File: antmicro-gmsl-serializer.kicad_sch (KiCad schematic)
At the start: 0 parts

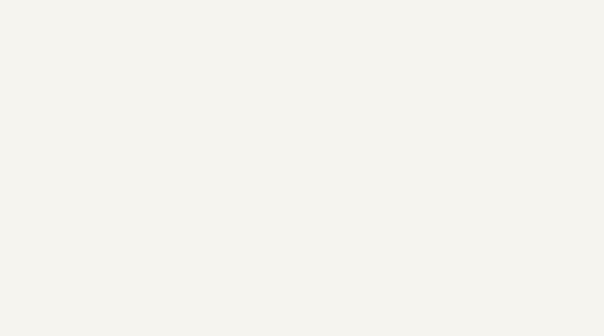
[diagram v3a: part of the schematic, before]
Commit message: Import layer stack, add mounting points
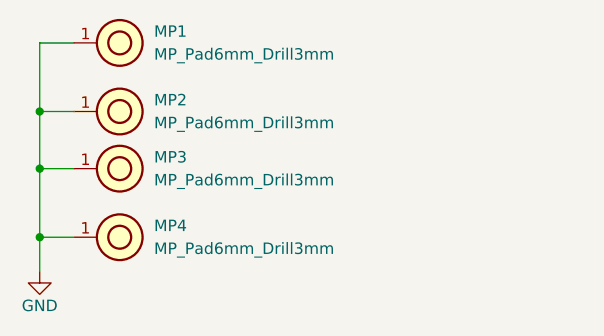
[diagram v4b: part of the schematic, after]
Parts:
- added MP1, MP2, MP3, MP4: MP_Pad6mm_Drill3mm, antmicro-footprints:MP_Pad6mm_Drill3mm, symbol antmicroMechanicalParts:MP_Pad6mm_Drill3mm
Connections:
- new net GND: MP1.1, MP2.1, MP3.1, MP4.1
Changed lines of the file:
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@@
     (comment 1 "www.antmicro.com")
+  )
+  (junction (at 24.13 157.48) (diameter 0) (color 0 0 0 0)
+  )
+  (junction (at 24.13 143.51) (diameter 0) (color 0 0 0 0)
+  )
+  (junction (at 24.13 149.86) (diameter 0) (color 0 0 0 0)
+  )
+  (wire (pts (xy 27.94 135.89) (xy 24.13 135.89))
+    (stroke (width 0) (type default) (color 0 0 0 0))
+  )
+  (wire (pts (xy 24.13 157.48) (xy 24.13 161.29))
+    (stroke (width 0) (type default) (color 0 0 0 0))
+  )
+  (wire (pts (xy 27.94 143.51) (xy 24.13 143.51))
+    (stroke (width 0) (type default) (color 0 0 0 0))
+  )
+  (wire (pts (xy 24.13 135.89) (xy 24.13 143.51))
+    (stroke (width 0) (type default) (color 0 0 0 0))
+  )
+  (wire (pts (xy 24.13 143.51) (xy 24.13 149.86))
+    (stroke (width 0) (type default) (color 0 0 0 0))
+  )
+  (wire (pts (xy 27.94 157.48) (xy 24.13 157.48))
+    (stroke (width 0) (type default) (color 0 0 0 0))
+  )
+  (wire (pts (xy 27.94 149.86) (xy 24.13 149.86))
+    (stroke (width 0) (type default) (color 0 0 0 0))
+  )
+  (wire (pts (xy 24.13 149.86) (xy 24.13 157.48))
+    (stroke (width 0) (type default) (color 0 0 0 0))
   )
   (image (at 71.12 185.674) (scale 0.15)
@@
     )
   )
+  (symbol (lib_id "antmicroMechanicalParts:MP_Pad6mm_Drill3mm") (at 27.94 157.48 0) (unit 1)
+    (in_bom yes) (on_board yes) (fields_autoplaced)
+    (property "Reference" "MP4" (id 0) (at 36.83 156.2099 0)
+      (effects (font (size 1.27 1.27) (thickness 0.15)) (justify left))
+    )
+    (property "Value" "MP_Pad6mm_Drill3mm" (id 1) (at 36.83 158.7499 0)
+      (effects (font (size 1.27 1.27) (thickness 0.15)) (justify left))
+    )
+    (property "Footprint" "antmicro-footprints:MP_Pad6mm_Drill3mm" (id 2) (at 48.26 165.1 0)
+      (effects (font (size 1.27 1.27) (thickness 0.15)) (justify left bottom) hide)
+    )
+    (property "Datasheet" "" (id 3) (at 44.78 173.05 0)
+      (effects (font (size 1.27 1.27) (thickness 0.15)) (justify left bottom) hide)
+    )
+    (property "Author" "Antmicro" (id 4) (at 48.26 167.64 0)
+      (effects (font (size 1.27 1.27) (thickness 0.15)) (justify left bottom) hide)
+    )
+    (property "License" "Apache-2.0" (id 5) (at 48.26 170.18 0)
+      (effects (font (size 1.27 1.27) (thickness 0.15)) (justify left bottom) hide)
+    )
+    (pin "1")
+  )
+  (symbol (lib_id "antmicroMechanicalParts:MP_Pad6mm_Drill3mm") (at 27.94 135.89 0) (unit 1)
+    (in_bom yes) (on_board yes) (fields_autoplaced)
+    (property "Reference" "MP1" (id 0) (at 36.83 134.6199 0)
+      (effects (font (size 1.27 1.27) (thickness 0.15)) (justify left))
+    )
+    (property "Value" "MP_Pad6mm_Drill3mm" (id 1) (at 36.83 137.1599 0)
+      (effects (font (size 1.27 1.27) (thickness 0.15)) (justify left))
+    )
+    (property "Footprint" "antmicro-footprints:MP_Pad6mm_Drill3mm" (id 2) (at 48.26 143.51 0)
+      (effects (font (size 1.27 1.27) (thickness 0.15)) (justify left bottom) hide)
+    )
+    (property "Datasheet" "" (id 3) (at 44.78 151.46 0)
+      (effects (font (size 1.27 1.27) (thickness 0.15)) (justify left bottom) hide)
+    )
+    (property "Author" "Antmicro" (id 4) (at 48.26 146.05 0)
+      (effects (font (size 1.27 1.27) (thickness 0.15)) (justify left bottom) hide)
+    )
+    (property "License" "Apache-2.0" (id 5) (at 48.26 148.59 0)
+      (effects (font (size 1.27 1.27) (thickness 0.15)) (justify left bottom) hide)
+    )
+    (pin "1")
+  )
+  (symbol (lib_id "antmicroMechanicalParts:MP_Pad6mm_Drill3mm") (at 27.94 143.51 0) (unit 1)
+    (in_bom yes) (on_board yes) (fields_autoplaced)
+    (property "Reference" "MP2" (id 0) (at 36.83 142.2399 0)
+      (effects (font (size 1.27 1.27) (thickness 0.15)) (justify left))
+    )
+    (property "Value" "MP_Pad6mm_Drill3mm" (id 1) (at 36.83 144.7799 0)
+      (effects (font (size 1.27 1.27) (thickness 0.15)) (justify left))
+    )
+    (property "Footprint" "antmicro-footprints:MP_Pad6mm_Drill3mm" (id 2) (at 48.26 151.13 0)
+      (effects (font (size 1.27 1.27) (thickness 0.15)) (justify left bottom) hide)
+    )
+    (property "Datasheet" "" (id 3) (at 44.78 159.08 0)
+      (effects (font (size 1.27 1.27) (thickness 0.15)) (justify left bottom) hide)
+    )
+    (property "Author" "Antmicro" (id 4) (at 48.26 153.67 0)
+      (effects (font (size 1.27 1.27) (thickness 0.15)) (justify left bottom) hide)
+    )
+    (property "License" "Apache-2.0" (id 5) (at 48.26 156.21 0)
+      (effects (font (size 1.27 1.27) (thickness 0.15)) (justify left bottom) hide)
+    )
+    (pin "1")
+  )
+  (symbol (lib_id "antmicropower:GND") (at 24.13 161.29 0) (unit 1)
+    (in_bom yes) (on_board yes)
+    (property "Reference" "#PWR0157" (id 0) (at 33.02 163.83 0)
+      (effects (font (size 1.27 1.27) (thickness 0.15)) (justify left bottom) hide)
+    )
+    (property "Value" "GND" (id 1) (at 24.13 165.1 0)
+      (effects (font (size 1.27 1.27) (thickness 0.15)))
+    )
+    (property "Footprint" "" (id 2) (at 33.02 168.91 0)
+      (effects (font (size 1.27 1.27) (thickness 0.15)) (justify left bottom) hide)
+    )
+    (property "Datasheet" "" (id 3) (at 33.02 173.99 0)
+      (effects (font (size 1.27 1.27) (thickness 0.15)) (justify left bottom) hide)
+    )
+    (property "Author" "Antmicro" (id 4) (at 33.02 168.91 0)
+      (effects (font (size 1.27 1.27) (thickness 0.15)) (justify left bottom) hide)
+    )
+    (property "License" "Apache-2.0" (id 5) (at 33.02 171.45 0)
+      (effects (font (size 1.27 1.27) (thickness 0.15)) (justify left bottom) hide)
+    )
+    (pin "1")
+  )
+  (symbol (lib_id "antmicroMechanicalParts:MP_Pad6mm_Drill3mm") (at 27.94 149.86 0) (unit 1)
+    (in_bom yes) (on_board yes) (fields_autoplaced)
+    (property "Reference" "MP3" (id 0) (at 36.83 148.5899 0)
+      (effects (font (size 1.27 1.27) (thickness 0.15)) (justify left))
+    )
+    (property "Value" "MP_Pad6mm_Drill3mm" (id 1) (at 36.83 151.1299 0)
+      (effects (font (size 1.27 1.27) (thickness 0.15)) (justify left))
+    )
+    (property "Footprint" "antmicro-footprints:MP_Pad6mm_Drill3mm" (id 2) (at 48.26 157.48 0)
+      (effects (font (size 1.27 1.27) (thickness 0.15)) (justify left bottom) hide)
+    )
+    (property "Datasheet" "" (id 3) (at 44.78 165.43 0)
+      (effects (font (size 1.27 1.27) (thickness 0.15)) (justify left bottom) hide)
+    )
+    (property "Author" "Antmicro" (id 4) (at 48.26 160.02 0)
+      (effects (font (size 1.27 1.27) (thickness 0.15)) (justify left bottom) hide)
+    )
+    (property "License" "Apache-2.0" (id 5) (at 48.26 162.56 0)
+      (effects (font (size 1.27 1.27) (thickness 0.15)) (justify left bottom) hide)
+    )
+    (pin "1")
+  )
   (sheet (at 104.14 135.89) (size 24.13 16.51) (fields_autoplaced)
     (stroke (width 0.1524) (type solid) (color 0 0 0 0))
@@
       (reference "#PWR0156") (unit 1) (value "GND") (footprint "")
     )
+    (path "/dbc6a5c8-e07b-4555-8e22-6830187dd63a"
+      (reference "#PWR0157") (unit 1) (value "GND") (footprint "")
+    )
     (path "/a0eea618-ebab-4bb8-b0df-45f61b300adb/f8cefd89-08db-4a81-83f6-63a8def027b4"
       (reference "C1") (unit 1) (value "C_10u_25V_0603") (footprint "antmicro-footprints:C_0603_1608Metric")
@@
       (reference "L6") (unit 1) (value "L_470n_1A_Coilcraft-PFL1609") (footprint "antmicro-footprints:L_Coilcraft-PFL1609")
     )
+    (path "/63605c51-2022-4f6b-9058-88dfedbdecff"
+      (reference "MP1") (unit 1) (value "MP_Pad6mm_Drill3mm") (footprint "antmicro-footprints:MP_Pad6mm_Drill3mm")
+    )
+    (path "/ca9c560a-6711-473d-a88a-aa22e71f3187"
+      (reference "MP2") (unit 1) (value "MP_Pad6mm_Drill3mm") (footprint "antmicro-footprints:MP_Pad6mm_Drill3mm")
+    )
+    (path "/f94c92ad-f4d5-4e2c-8028-eceea0320c2b"
+      (reference "MP3") (unit 1) (value "MP_Pad6mm_Drill3mm") (footprint "antmicro-footprints:MP_Pad6mm_Drill3mm")
+    )
+    (path "/47b8f45e-ee53-4ca1-8e8b-7596e0e41912"
+      (reference "MP4") (unit 1) (value "MP_Pad6mm_Drill3mm") (footprint "antmicro-footprints:MP_Pad6mm_Drill3mm")
+    )
     (path "/5ec47368-f2bc-48df-ac04-8fe6feb94419/d0230d45-4e16-41f7-80fd-5f245a8c8940"

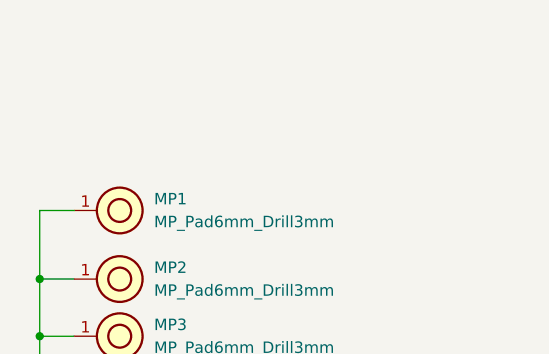
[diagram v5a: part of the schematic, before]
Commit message: Route 12V to 5V DC converter
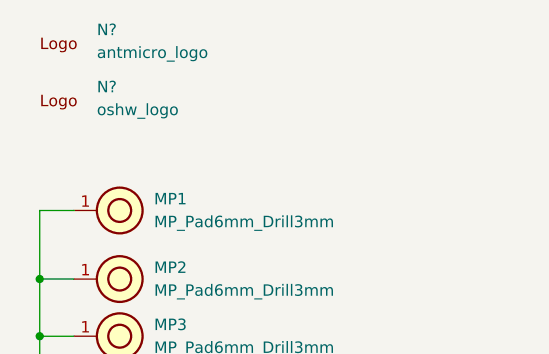
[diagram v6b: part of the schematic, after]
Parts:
- added N?: antmicro_logo, antmicro-footprints:antmicro-logo, symbol antmicroMechanicalParts:antmicro_logo
- added N?: oshw_logo, antmicro-footprints:oshw-logo, symbol antmicroMechanicalParts:oshw_logo
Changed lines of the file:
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@@
     (pin "1")
+  )
+  (symbol (lib_id "antmicroMechanicalParts:antmicro_logo") (at 24.13 118.11 0) (unit 1)
+    (in_bom no) (on_board yes) (fields_autoplaced)
+    (property "Reference" "N?" (id 0) (at 30.48 115.8175 0)
+      (effects (font (size 1.27 1.27) (thickness 0.15)) (justify left))
+    )
+    (property "Value" "antmicro_logo" (id 1) (at 30.48 118.3575 0)
+      (effects (font (size 1.27 1.27) (thickness 0.15)) (justify left))
+    )
+    (property "Footprint" "antmicro-footprints:antmicro-logo" (id 2) (at 39.37 128.27 0)
+      (effects (font (size 1.27 1.27) (thickness 0.15)) (justify left bottom) hide)
+    )
+    (property "Datasheet" "" (id 3) (at 39.37 130.81 0)
+      (effects (font (size 1.27 1.27) (thickness 0.15)) (justify left bottom) hide)
+    )
+    (property "MPN" "" (id 4) (at 24.13 118.11 0)
+      (effects (font (size 1.27 1.27)) hide)
+    )
+    (property "Manufacturer" "" (id 5) (at 39.37 138.43 0)
+      (effects (font (size 1.27 1.27) (thickness 0.15)) (justify left bottom) hide)
+    )
+    (property "Author" "Antmicro" (id 6) (at 39.37 133.35 0)
+      (effects (font (size 1.27 1.27) (thickness 0.15)) (justify left bottom) hide)
+    )
+    (property "License" "Apache-2.0" (id 7) (at 39.37 135.89 0)
+      (effects (font (size 1.27 1.27) (thickness 0.15)) (justify left bottom) hide)
+    )
+  )
+  (symbol (lib_id "antmicroMechanicalParts:oshw_logo") (at 24.13 124.46 0) (unit 1)
+    (in_bom no) (on_board yes) (fields_autoplaced)
+    (property "Reference" "N?" (id 0) (at 30.48 122.1675 0)
+      (effects (font (size 1.27 1.27) (thickness 0.15)) (justify left))
+    )
+    (property "Value" "oshw_logo" (id 1) (at 30.48 124.7075 0)
+      (effects (font (size 1.27 1.27) (thickness 0.15)) (justify left))
+    )
+    (property "Footprint" "antmicro-footprints:oshw-logo" (id 2) (at 39.37 134.62 0)
+      (effects (font (size 1.27 1.27) (thickness 0.15)) (justify left bottom) hide)
+    )
+    (property "Datasheet" "" (id 3) (at 39.37 137.16 0)
+      (effects (font (size 1.27 1.27) (thickness 0.15)) (justify left bottom) hide)
+    )
+    (property "Author" "Antmicro" (id 4) (at 39.37 139.7 0)
+      (effects (font (size 1.27 1.27) (thickness 0.15)) (justify left bottom) hide)
+    )
+    (property "License" "Apache-2.0" (id 5) (at 39.37 142.24 0)
+      (effects (font (size 1.27 1.27) (thickness 0.15)) (justify left bottom) hide)
+    )
+    (property "MPN" "" (id 6) (at 24.13 124.46 0)
+      (effects (font (size 1.27 1.27)) hide)
+    )
+    (property "Manufacturer" "" (id 7) (at 39.37 144.78 0)
+      (effects (font (size 1.27 1.27) (thickness 0.15)) (justify left bottom) hide)
+    )
   )
   (symbol (lib_id "antmicroMechanicalParts:MP_Pad6mm_Drill3mm") (at 27.94 143.51 0) (unit 1)
@@
       (reference "MP4") (unit 1) (value "MP_Pad6mm_Drill3mm") (footprint "antmicro-footprints:MP_Pad6mm_Drill3mm")
     )
+    (path "/99170140-c977-4704-808b-29f1a020f74c"
+      (reference "N?") (unit 1) (value "antmicro_logo") (footprint "antmicro-footprints:antmicro-logo")
+    )
+    (path "/b9465c26-dfee-47c8-a104-959558705dc8"
+      (reference "N?") (unit 1) (value "oshw_logo") (footprint "antmicro-footprints:oshw-logo")
+    )
     (path "/5ec47368-f2bc-48df-ac04-8fe6feb94419/d0230d45-4e16-41f7-80fd-5f245a8c8940"

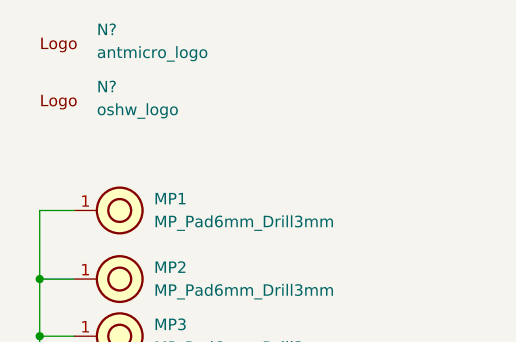
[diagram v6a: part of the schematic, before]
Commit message: Remove R15 and anotate schematic
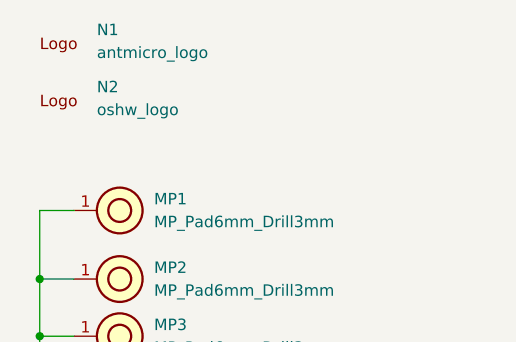
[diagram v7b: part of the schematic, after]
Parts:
- N1: renamed from N?; footprint antmicro-footprints:antmicro-logo -> antmicro-footprints:antmicro-logo_scaled_12mm
- gave numbers to parts that had none: 1
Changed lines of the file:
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@@
   (symbol (lib_id "antmicroMechanicalParts:antmicro_logo") (at 24.13 118.11 0) (unit 1)
     (in_bom no) (on_board yes) (fields_autoplaced)
-    (property "Reference" "N?" (id 0) (at 30.48 115.8175 0)
+    (property "Reference" "N1" (id 0) (at 30.48 115.8175 0)
       (effects (font (size 1.27 1.27) (thickness 0.15)) (justify left))
     )
@@
       (effects (font (size 1.27 1.27) (thickness 0.15)) (justify left))
     )
-    (property "Footprint" "antmicro-footprints:antmicro-logo" (id 2) (at 39.37 128.27 0)
+    (property "Footprint" "antmicro-footprints:antmicro-logo_scaled_12mm" (id 2) (at 39.37 128.27 0)
       (effects (font (size 1.27 1.27) (thickness 0.15)) (justify left bottom) hide)
     )
@@
   (symbol (lib_id "antmicroMechanicalParts:oshw_logo") (at 24.13 124.46 0) (unit 1)
     (in_bom no) (on_board yes) (fields_autoplaced)
-    (property "Reference" "N?" (id 0) (at 30.48 122.1675 0)
+    (property "Reference" "N2" (id 0) (at 30.48 122.1675 0)
       (effects (font (size 1.27 1.27) (thickness 0.15)) (justify left))
     )
@@
     )
     (path "/99170140-c977-4704-808b-29f1a020f74c"
-      (reference "N?") (unit 1) (value "antmicro_logo") (footprint "antmicro-footprints:antmicro-logo")
+      (reference "N1") (unit 1) (value "antmicro_logo") (footprint "antmicro-footprints:antmicro-logo_scaled_12mm")
     )
     (path "/b9465c26-dfee-47c8-a104-959558705dc8"
-      (reference "N?") (unit 1) (value "oshw_logo") (footprint "antmicro-footprints:oshw-logo")
+      (reference "N2") (unit 1) (value "oshw_logo") (footprint "antmicro-footprints:oshw-logo")
     )
     (path "/5ec47368-f2bc-48df-ac04-8fe6feb94419/d0230d45-4e16-41f7-80fd-5f245a8c8940"
@@
       (reference "R14") (unit 1) (value "R_0R_22.4A_0603") (footprint "antmicro-footprints:R_0603_1608Metric")
     )
-    (path "/a0eea618-ebab-4bb8-b0df-45f61b300adb/acaed7cf-fad2-49dd-a81a-936a94f5ef77"
-      (reference "R15") (unit 1) (value "R_0R_22.4A_0603") (footprint "antmicro-footprints:R_0603_1608Metric")
-    )
     (path "/a0eea618-ebab-4bb8-b0df-45f61b300adb/83c06f78-e70b-4b2e-bc34-469ec4d274e0"
